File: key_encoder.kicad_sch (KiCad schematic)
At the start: 0 parts

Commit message: modificato:             analog_synth.kicad_pro 	modificato:             key_encoder.kicad_sch 	modificato:             vca.kicad_pro 	modificato:             vca.kicad_sch 	nuovo file:             vca.net 	modificato:             vcf.kicad_sch
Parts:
- added C10, C11: 10nF, symbol Device:C_Small
- added C12: 1uF, symbol Device:C_Small
- added C13: 210nF, symbol Device:C_Small
- added C14: 5nF, symbol Device:C_Small
- added J1: KEY_2, symbol Connector_Generic:Conn_01x08
- added J2: KEY_1, symbol Connector_Generic:Conn_01x08
- added R38, R39, R41, R43, R45: 10k, symbol Device:R
- added R40: 470k, symbol Device:R_Variable
- added R42, R46: 100k, symbol Device:R
- added R44: 470, symbol Device:R
- added R47: 1m, symbol Device:R_Variable
- added SW2: SW_01, symbol Switch:SW_SPST
- added SW3: Push_01, symbol Switch:SW_Push
- added SW4: DEV_01, symbol Switch:SW_DPDT_x2
- added U10: 4049, symbol 4xxx:4049
- added U11: 4023, symbol 4xxx:4023
- added U12, U15: CD4051B, symbol Analog_Switch:CD4051B
- added U13, U14: 4042, symbol 4xxx_IEEE:4042
- added U16: 4024, symbol 4xxx_IEEE:4024
- added U17, U18, U19: 4001, symbol 4xxx:4001
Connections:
- new net: R45.1, U18.10, U18.5, U18.6
- new net: C14.2, R45.2, U18.8
- new net: J2.1 (Pin_1), U15.4 (X7)
- new net: J2.2 (Pin_2), U15.2 (X6)
- new net: J2.3 (Pin_3), U15.5 (X5)
- new net: J2.4 (Pin_4), U15.1 (X4)
- new net: J2.5 (Pin_5), U15.12 (X3)
- new net: J2.6 (Pin_6), U15.15 (X2)
- new net: J2.7 (Pin_7), U15.14 (X1)
- new net: J2.8 (Pin_8), U15.13 (X0)
- new net: R46.1, SW4.2 (B), U18.9
- new net: R46.2, R47.1
- new net: C10.2, R42.1, U19.5, U19.6
- new net: U16.1 (~{CLK}), U17.11, U18.3
- new net: U11.6, U16.2 (MR)
- new net: R43.1, U15.3 (X), U17.2
- new net: C10.1, U19.3
- new net: C11.1, R38.1, U17.1
- new net: U17.3, U17.5, U17.6, U19.2
- new net: J1.5 (Pin_5), U12.1 (X4)
- new net: J1.4 (Pin_4), U12.12 (X3)
- new net: J1.1 (Pin_1), U12.13 (X0)
- new net: J1.2 (Pin_2), U12.14 (X1)
- new net: J1.3 (Pin_3), U12.15 (X2)
- new net: J1.7 (Pin_7), U12.2 (X6)
- new net: R44.2, U12.3 (X)
- new net: J1.8 (Pin_8), U12.4 (X7)
- new net: J1.6 (Pin_6), U12.5 (X5)
- new net: R41.2, SW2.1 (A), SW3.1, U18.13
- new net: C13.1, SW4.1 (A), U17.4
- new net: C13.2, SW4.3 (C)
- new net: C11.2, C12.1, U17.10
- new net: C12.2, R40.2, U18.12
- new net: C14.1, U17.12, U17.13, U18.1, U18.2, U18.4
- new net: R39.1, U17.8, U17.9, U18.11
- new net: R39.2, R40.1
- new net: U11.10, U11.3, U11.4, U11.5
- new net +12V: R41.1, R44.1, U12.16 (VDD), U15.16 (VDD)
- new net GNDREF: R38.2, R42.2, R43.2, R47.2, SW2.2 (B), SW3.2, U11.1, U11.2, U11.8, U12.6 (INH), U12.8 (VSS), U15.8 (VSS), U19.12, U19.13, U19.8, U19.9
- new net OUT_PULSE: U19.1, U19.4
- no-connect marks 0 -> 2
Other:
- title: (none) -> Encoder digitale per tastiera musicale 49 Tast

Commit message: modificato:             key_encoder.kicad_sch
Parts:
- added C15: 2.2uF, symbol Device:C_Polarized_Small
- added D2: 1N4148, Diode_THT:D_DO-35_SOD27_P7.62mm_Horizontal, symbol Diode:1N4148
- added R48, R49, R51, R54, R57, R60, R63, R66, R67, R68, R69: 47k, symbol Device:R
- added R50, R55: 10k, symbol Device:R_Trim
- added R52, R58, R61, R64: 20k, symbol Device:R_Trim
- added R53: 100k, symbol Device:R
- added R56, R59, R65: 10k, symbol Device:R
- added R62: 5.6k, symbol Device:R
- added RV4: 100k, symbol Device:R_Potentiometer
- added U20, U9: LM324, symbol Amplifier_Operational:LM324
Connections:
- net +12V: now also R66.1
- net GNDREF: now also C15.2, D2.1 (K), R69.2
- new net: R62.1, R63.1, U20.12 (+)
- new net: R63.2, R64.1
- new net: R60.2, R61.1
- new net: R54.1, R59.2, U20.9 (-)
- new net: R54.2, R55.1
- new net: R53.1, R56.2, U20.7
- new net: R49.1, R53.2, U20.6 (-)
- new net: R57.2, R58.1
- new net: R48.1, R51.1, U20.5 (+)
- new net: R48.2, U20.1, U20.2 (-)
- new net: R68.2, R69.1, RV4.3
- new net: R49.2, R50.1
- new net: R51.2, R52.1
- new net: R60.1, R65.2, U20.13 (-)
- new net: C15.1, D2.2 (A), R66.2, R67.1
- new net: R59.1, R62.2, U20.8
- new net: R67.2, R68.1, RV4.1
- new net: R56.1, R57.1, U20.10 (+)
- new net: RV4.2, U20.3 (+)
- new net ANALOG_OUT: R65.1, U20.14
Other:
- moved on the sheet: C14, R45, R46, R47, U17D, U18A, U18B, U18C

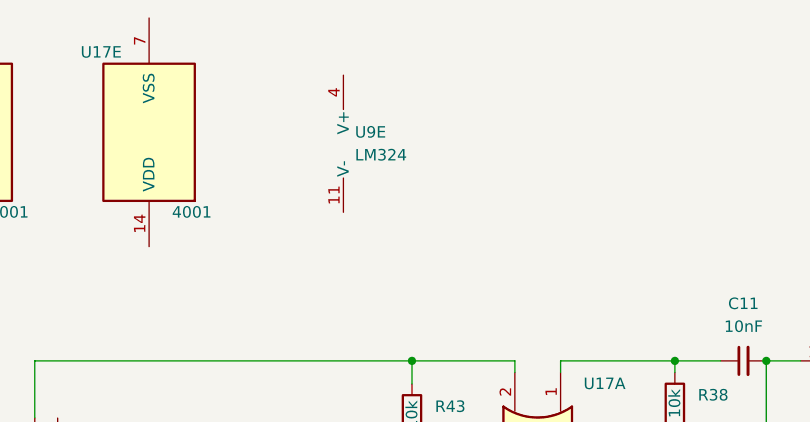
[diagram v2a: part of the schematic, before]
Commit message: eliminato:              adsr.kicad_pcb     eliminato:              adsr.kicad_pro 	modificato:             analog_synth.kicad_pcb 	nuovo file:             analog_synth.net 	eliminato:              audio_mixer.kicad_pcb 	eliminato:              audio_mixer.kicad_pro 	eliminato:              key_encoder.kicad_pcb 	eliminato:              key_encoder.kicad_pro 	modificato:             key_encoder.kicad_sch 	eliminato:              lfo.kicad_pcb 	eliminato:              lfo.kicad_pro 	eliminato:              noise_gen.kicad_pcb 	eliminato:              noise_gen.kicad_pro 	eliminato:              vca.kicad_pcb 	eliminato:              vca.kicad_prl 	eliminato:              vca.kicad_pro 	modificato:             vca.kicad_sch 	eliminato:              vca.net 	eliminato:              vcf.kicad_pcb 	eliminato:              vcf.kicad_prl 	eliminato:              vcf.kicad_pro 	modificato:             vcf.kicad_sch 	eliminato:              vco.kicad_pcb 	eliminato:              vco.kicad_pro
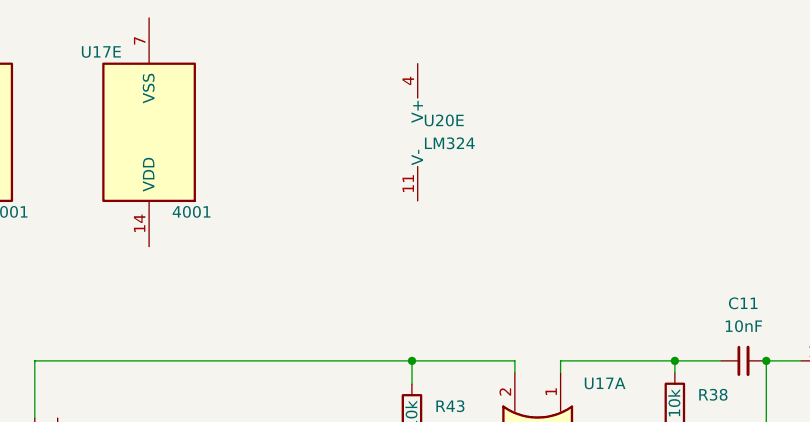
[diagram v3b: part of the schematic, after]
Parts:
- removed U9: LM324, symbol Amplifier_Operational:LM324
- added unit 5 of U20
- R38, R39, R40, R41, R42, R43, R44, R45, R46, R47, R48, R49, R51, R53, R54, R56, R57, R59, R60, R62, R63, R65, R66, R67, R68, R69, RV4: footprint (none) -> Resistor_SMD:R_0805_2012Metric
- R50, R52, R55, R58, R61, R64: footprint (none) -> Potentiometer_THT:Potentiometer_Bourns_3009P_Horizontal
- U10, U11, U13, U14, U16, U17, U18, U19, U20: footprint (none) -> Package_DIP:DIP-14_W7.62mm_Socket
- U12, U15: footprint (none) -> Package_DIP:DIP-16_W7.62mm_Socket

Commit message: modificato:             analog_synth.kicad_pcb 	modificato:             key_encoder.kicad_sch
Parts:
- added U21, U22: CD4066BE, Package_DIP:DIP-14_W7.62mm_Socket, symbol Analog_Switch:CD4066BE
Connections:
- net GNDREF: now also U13.6 (E1), U13.8 (Vss), U14.6 (E1), U14.8 (Vss), U21.10, U21.2, U21.3, U21.9, U22.10, U22.9
- net at R61.2: now also U22.11
- net at R64.2: now also U22.8
- net at U16.1 (~{CLK}), U17.11, U18.3: now also U15.6 (INH)
- net at U16.11 (Q1): now also U14.7, U15.10 (B)
- net at U16.12 (Q0): now also U11.13, U14.4, U15.11 (A)
- net at U16.4 (Q5): now also U11.11, U12.9 (C), U13.14
- net at U16.5 (Q4): now also U11.12, U12.10 (B), U13.13
- net at U16.6 (Q3): now also U12.11 (A), U13.7
- net at U16.9 (Q2): now also U13.4, U15.9 (C)
- net at U13.5 (E0): now also U14.5 (E0), U17.3, U17.5, U17.6, U19.2
- net at R58.2: now also U21.8
- net at R52.2: now also U21.11
- net at R55.2: now also U21.4
- net at R50.2: now also U21.1
- no-connect marks 2 -> 5
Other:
- moved on the sheet: C14, R45, R46, R47, U10A, U10B, U10C, U10D, U10E, U10F, U17D, U18A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
